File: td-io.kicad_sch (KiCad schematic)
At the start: 156 parts, among them J1 USB_A, J2 USB_B, J3 JAMMA_Edge, J4 Conn_Coaxial_x2, J5 DB15_Female_HighDensity_Mount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, J6 Conn_02x04_Top_Bottom, J7 Conn_02x17_Odd_Even, J8 Conn_01x05_Male, J9 Conn_01x04_Male, Q1 AO4818B, Q2 AO4818B, Q3 AO4818B, Q4 2N7002NXBKR, Q5 2N7002NXBKR, Q6 2N7002NXBKR, SW1 SW_DPDT_x2, SW2 SW_DPDT_x2, SW3 SW_DPDT_x2, U1 TPA3138D2, U10 Pico, U11 MAX860, U12 CPC1017N, U13 74LS165, U14 TPS259620, U15 LM2903, U16 PCA9306D, U2 ISL3175EIBZ-T, U3 ADA4861-3, U4 74LS86, U5 AT24CS01-SSHM, U6 74LS165, U7 TPS568230, U8 74LS165, U9 74LS165

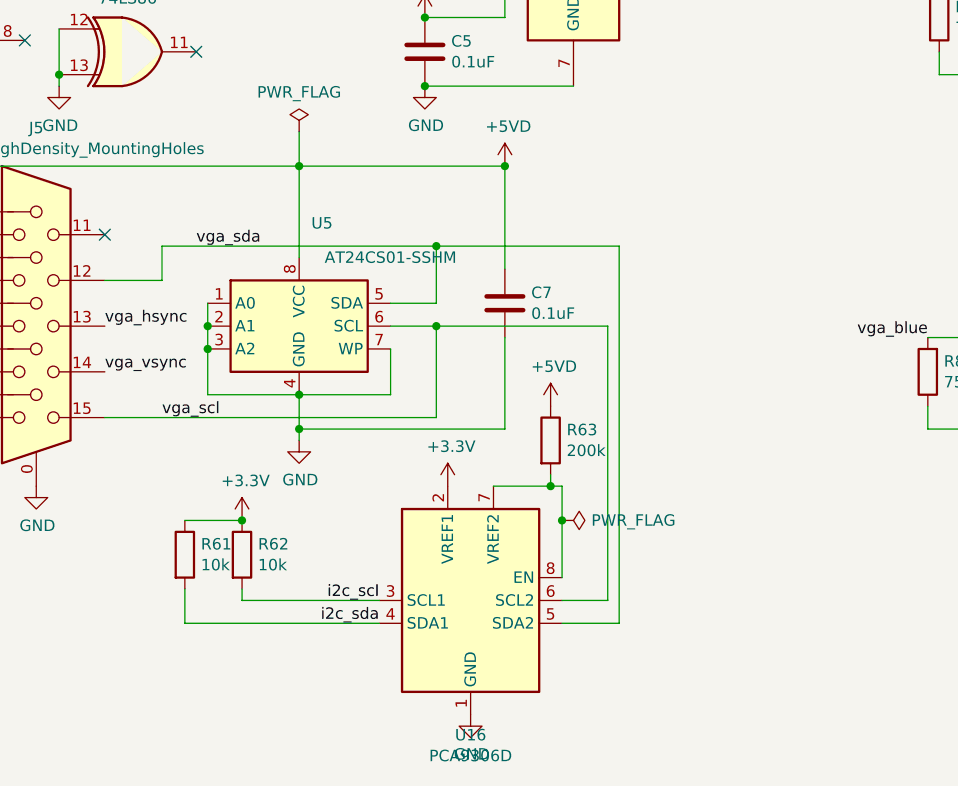
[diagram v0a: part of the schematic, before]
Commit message: drop i2c rom
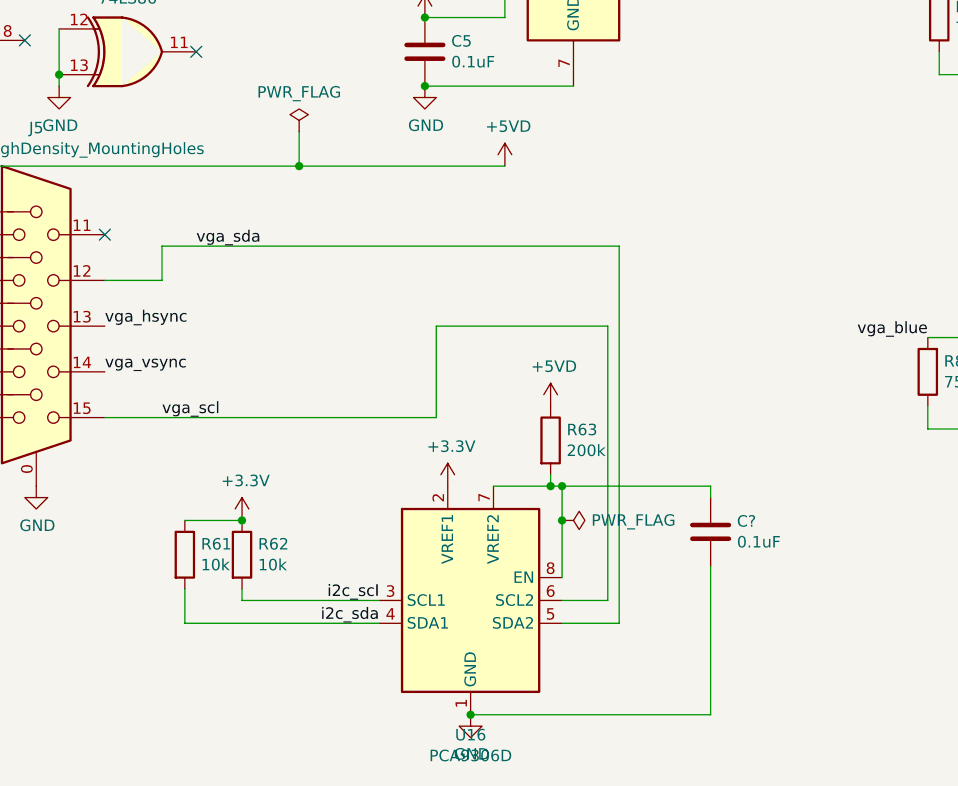
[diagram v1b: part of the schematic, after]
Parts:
- removed C7: 0.1uF, Capacitor_SMD:C_0805_2012Metric, symbol Device:C
- removed U5: AT24CS01-SSHM, Package_SO:SOIC-8_3.9x4.9mm_P1.27mm, symbol Memory_EEPROM:AT24CS01-SSHM
- added C?: 0.1uF, Capacitor_SMD:C_0805_2012Metric, symbol Device:C
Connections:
- net GND: now also C?.2
- net at R63.2, U16.7 (VREF2), U16.8 (EN): now also C?.1

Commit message: some pcb layout action
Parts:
- gave numbers to parts that had none: 1
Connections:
- net at F5.2, Q2.7 (D1), Q2.8 (D1): now also D4.2 (K); no longer D3.1 (K)
- net at F3.2, Q3.5 (D2), Q3.6 (D2): now also D3.1 (K); no longer D4.2 (K)
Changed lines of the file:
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@@
   (junction (at 524.51 62.23) (diameter 0) (color 0 0 0 0)
   )
-  (junction (at 481.33 143.51) (diameter 0) (color 0 0 0 0)
-  )
   (junction (at 506.73 58.42) (diameter 0) (color 0 0 0 0)
   )
@@
   (junction (at 419.1 45.72) (diameter 0) (color 0 0 0 0)
   )
+  (junction (at 481.33 143.51) (diameter 0) (color 0 0 0 0)
+  )
   (junction (at 41.91 367.03) (diameter 0) (color 0 0 0 0)
   )
@@
   (junction (at 405.13 210.82) (diameter 0) (color 0 0 0 0)
   )
-  (junction (at 452.755 182.88) (diameter 0) (color 0 0 0 0)
-  )
   (junction (at 207.01 378.46) (diameter 0) (color 0 0 0 0)
   )
@@
   (junction (at 87.63 95.25) (diameter 0) (color 0 0 0 0)
   )
+  (junction (at 452.755 182.88) (diameter 0) (color 0 0 0 0)
+  )
   (junction (at 222.25 363.22) (diameter 0) (color 0 0 0 0)
   )
@@
     (stroke (width 0) (type default) (color 0 0 0 0))
   )
+  (wire (pts (xy 452.755 182.88) (xy 465.455 182.88))
+    (stroke (width 0) (type default) (color 0 0 0 0))
+  )
   (wire (pts (xy 472.44 143.51) (xy 472.44 127))
     (stroke (width 0) (type default) (color 0 0 0 0))
@@
     (stroke (width 0) (type default) (color 0 0 0 0))
   )
+  (wire (pts (xy 495.935 166.37) (xy 495.935 143.51))
+    (stroke (width 0) (type default) (color 0 0 0 0))
+  )
   (wire (pts (xy 38.1 21.59) (xy 38.1 46.99))
     (stroke (width 0) (type default) (color 0 0 0 0))
@@
     (stroke (width 0) (type default) (color 0 0 0 0))
   )
+  (wire (pts (xy 495.935 166.37) (xy 511.175 166.37))
+    (stroke (width 0) (type default) (color 0 0 0 0))
+  )
   (wire (pts (xy 510.54 127) (xy 510.54 142.875))
     (stroke (width 0) (type default) (color 0 0 0 0))
@@
     (stroke (width 0) (type default) (color 0 0 0 0))
   )
+  (wire (pts (xy 505.46 142.875) (xy 499.745 142.875))
+    (stroke (width 0) (type default) (color 0 0 0 0))
+  )
   (wire (pts (xy 560.07 44.45) (xy 560.07 48.26))
     (stroke (width 0) (type default) (color 0 0 0 0))
@@
     (stroke (width 0) (type default) (color 0 0 0 0))
   )
-  (wire (pts (xy 452.755 182.88) (xy 470.535 182.88))
-    (stroke (width 0) (type default) (color 0 0 0 0))
-  )
   (wire (pts (xy 388.62 182.88) (xy 388.62 173.99))
     (stroke (width 0) (type default) (color 0 0 0 0))
@@
     (stroke (width 0) (type default) (color 0 0 0 0))
   )
-  (wire (pts (xy 501.65 143.51) (xy 501.65 142.875))
-    (stroke (width 0) (type default) (color 0 0 0 0))
-  )
   (wire (pts (xy 444.5 50.8) (xy 444.5 45.72))
     (stroke (width 0) (type default) (color 0 0 0 0))
@@
     (stroke (width 0) (type default) (color 0 0 0 0))
   )
-  (wire (pts (xy 470.535 166.37) (xy 470.535 182.88))
+  (wire (pts (xy 465.455 165.1) (xy 465.455 182.88))
     (stroke (width 0) (type default) (color 0 0 0 0))
   )
@@
     (stroke (width 0) (type default) (color 0 0 0 0))
   )
+  (wire (pts (xy 495.935 143.51) (xy 481.33 143.51))
+    (stroke (width 0) (type default) (color 0 0 0 0))
+  )
   (wire (pts (xy 161.29 368.3) (xy 161.29 370.84))
     (stroke (width 0) (type default) (color 0 0 0 0))
@@
     (stroke (width 0) (type default) (color 0 0 0 0))
   )
-  (wire (pts (xy 481.33 143.51) (xy 501.65 143.51))
-    (stroke (width 0) (type default) (color 0 0 0 0))
-  )
   (wire (pts (xy 208.28 326.39) (xy 208.28 339.09))
     (stroke (width 0) (type default) (color 0 0 0 0))
@@
     (stroke (width 0) (type default) (color 0 0 0 0))
   )
+  (wire (pts (xy 499.745 165.1) (xy 465.455 165.1))
+    (stroke (width 0) (type default) (color 0 0 0 0))
+  )
   (wire (pts (xy 60.96 97.79) (xy 60.96 86.36))
     (stroke (width 0) (type default) (color 0 0 0 0))
@@
     (stroke (width 0) (type default) (color 0 0 0 0))
   )
-  (wire (pts (xy 470.535 166.37) (xy 511.175 166.37))
-    (stroke (width 0) (type default) (color 0 0 0 0))
-  )
   (wire (pts (xy 276.86 90.17) (xy 280.67 90.17))
     (stroke (width 0) (type default) (color 0 0 0 0))
@@
     (stroke (width 0) (type default) (color 0 0 0 0))
   )
-  (wire (pts (xy 501.65 142.875) (xy 505.46 142.875))
-    (stroke (width 0) (type default) (color 0 0 0 0))
-  )
   (wire (pts (xy 110.49 402.59) (xy 137.16 402.59))
     (stroke (width 0) (type default) (color 0 0 0 0))
@@
     (stroke (width 0) (type default) (color 0 0 0 0))
   )
+  (wire (pts (xy 499.745 142.875) (xy 499.745 165.1))
+    (stroke (width 0) (type default) (color 0 0 0 0))
+  )
   (wire (pts (xy 50.8 21.59) (xy 57.15 21.59))
     (stroke (width 0) (type default) (color 0 0 0 0))
@@
   (symbol (lib_id "Device:C") (at 137.16 382.27 0) (unit 1)
     (in_bom yes) (on_board yes)
-    (property "Reference" "C?" (id 0) (at 140.081 381.1016 0)
+    (property "Reference" "C7" (id 0) (at 140.081 381.1016 0)
       (effects (font (size 1.27 1.27)) (justify left))
     )
@@
   (symbol (lib_id "power:GND") (at 100.33 285.75 0) (unit 1)
     (in_bom yes) (on_board yes)
-    (property "Reference" "#PWR?" (id 0) (at 100.33 292.1 0)
+    (property "Reference" "#PWR0127" (id 0) (at 100.33 292.1 0)
       (effects (font (size 1.27 1.27)) hide)
     )
@@
       (reference "#PWR0126") (unit 1) (value "+5V") (footprint "")
     )
+    (path "/ea8e2432-37dd-41a8-b7a1-d69d5340706c"
+      (reference "#PWR0127") (unit 1) (value "GND") (footprint "")
+    )
     (path "/00000000-0000-0000-0000-000060061134"
       (reference "#PWR0128") (unit 1) (value "GND") (footprint "")
@@
       (reference "#PWR0179") (unit 1) (value "+3.3V") (footprint "")
     )
-    (path "/ea8e2432-37dd-41a8-b7a1-d69d5340706c"
-      (reference "#PWR?") (unit 1) (value "GND") (footprint "")
-    )
     (path "/00000000-0000-0000-0000-000060392eef"
       (reference "C1") (unit 1) (value "1uF") (footprint "Capacitor_SMD:C_0805_2012Metric")
@@
       (reference "C6") (unit 1) (value "0.1uF") (footprint "Capacitor_SMD:C_0805_2012Metric")
     )
+    (path "/6fed136c-eb32-480f-be11-cce40318add5"
+      (reference "C7") (unit 1) (value "0.1uF") (footprint "Capacitor_SMD:C_0805_2012Metric")
+    )
     (path "/00000000-0000-0000-0000-000060403e55"
       (reference "C8") (unit 1) (value "1uF") (footprint "Capacitor_SMD:C_0805_2012Metric")
@@
       (reference "C40") (unit 1) (value "1uF") (footprint "Capacitor_SMD:C_0805_2012Metric")
     )
-    (path "/6fed136c-eb32-480f-be11-cce40318add5"
-      (reference "C?") (unit 1) (value "0.1uF") (footprint "Capacitor_SMD:C_0805_2012Metric")
-    )
     (path "/00000000-0000-0000-0000-000061046d38"

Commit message: finish layout
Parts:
- removed JP1: Jumper_NC_Small, Jumper:SolderJumper-2_P1.3mm_Bridged_RoundedPad1.0x1.5mm, symbol Device:Jumper_NC_Small
- removed R2: 400k, Resistor_SMD:R_0805_2012Metric, symbol Device:R
- removed R3: 1k, Resistor_SMD:R_0805_2012Metric, symbol Device:R
- removed U14: TPS259620, Package_SO:SOIC-8-1EP_3.9x4.9mm_P1.27mm_EP2.41x3.3mm_ThermalVias, symbol td-io:TPS259631
- added F6: Polyfuse, Resistor_SMD:R_1812_4532Metric, symbol Device:Polyfuse
- RV1: symbol Device:R_POT_Dual -> Device:R_Potentiometer_Dual
- U10: footprint td-io:RPi_Pico_SMD -> RPi_Pico:RPi_Pico_SMD_TH
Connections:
- net +5V: now also F6.2
- net +5VD: now also D2.1
- net +5VL: now also F6.1
- no-connect marks 64 -> 63

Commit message: update to new psu
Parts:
- removed C10: 1uF, Capacitor_SMD:C_0805_2012Metric, symbol Device:C
- removed C11, C29: 0.1uF, Capacitor_SMD:C_0805_2012Metric, symbol Device:C
- removed C12, C9: 100uF, Capacitor_SMD:C_1210_3225Metric, symbol Device:C
- removed L1: 1.5uH, Inductor_SMD:L_Bourns_SRP7028A_7.3x6.6mm, symbol Device:L
- removed R20: 300k, Resistor_SMD:R_0805_2012Metric, symbol Device:R
- removed R21: 43k, Resistor_SMD:R_0805_2012Metric, symbol Device:R
- removed R32: 1k, Resistor_SMD:R_0805_2012Metric, symbol Device:R
- removed R33: 220, Resistor_SMD:R_0805_2012Metric, symbol Device:R
- removed U7: TPS568230, td-io:RJE-20, symbol td-io:TPS568230
- D2: Digikey (none) -> BAT54CFSCT-ND
- J8: value Conn_01x05_Male -> DNP
- R11, R12, R13: JLCPCB (none) -> C17630; LCSC (none) -> C17630
- R61, R62: Digikey (none) -> 311-10.0KCRCT-ND
- R63: Digikey (none) -> 311-200KCRCT-ND; JLCPCB (none) -> C17539; LCSC (none) -> C17539
- U13, U6, U8, U9: value 74LS165 -> 74LV165
- U16: Digikey (none) -> 568-4215-1-ND
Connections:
- no-connect marks 63 -> 61
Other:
- added sheet JVS Power (jvs-power.kicad_sch)

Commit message: small fixes
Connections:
- net +3V3: no longer R22.1, R23.1, R24.1, R27.1, R28.1, R29.1, R30.1, R31.1, R34.1, R35.1, R36.1, R37.1, R38.1, R39.1, R40.1, R41.1, R42.1, R43.1, R44.1, R45.1, R46.1, R47.1, R48.1, R49.1, R56.1, R57.1, R58.1, U13.14 (D3), U13.3 (D4), U13.4 (D5), U13.5 (D6), U13.6 (D7)
- net +5V: now also R22.1, R23.1, R24.1, R27.1, R28.1, R29.1, R30.1, R31.1, R34.1, R35.1, R36.1, R37.1, R38.1, R39.1, R40.1, R41.1, R42.1, R43.1, R44.1, R45.1, R46.1, R47.1, R48.1, R49.1, R56.1, R57.1, R58.1, U13.14 (D3), U13.3 (D4), U13.4 (D5), U13.5 (D6), U13.6 (D7)

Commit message: re test zones
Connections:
- net +3V3: now also U13.14 (D3), U13.3 (D4), U13.4 (D5), U13.5 (D6), U13.6 (D7)
- net +5V: no longer U13.14 (D3), U13.3 (D4), U13.4 (D5), U13.5 (D6), U13.6 (D7)
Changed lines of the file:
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@@
   (junction (at 41.91 369.57) (diameter 0) (color 0 0 0 0)
   )
+  (junction (at 40.64 21.59) (diameter 0) (color 0 0 0 0)
+  )
   (junction (at 175.26 360.68) (diameter 0) (color 0 0 0 0)
   )
@@
   (junction (at 102.87 172.72) (diameter 0) (color 0 0 0 0)
   )
-  (junction (at 46.6093 21.59) (diameter 0) (color 0 0 0 0)
-  )
   (junction (at 138.43 105.41) (diameter 0) (color 0 0 0 0)
   )
@@
   (junction (at 105.41 325.12) (diameter 0) (color 0 0 0 0)
   )
-  (junction (at 50.8 21.59) (diameter 0) (color 0 0 0 0)
-  )
   (junction (at 513.08 102.87) (diameter 0) (color 0 0 0 0)
   )
@@
   (junction (at 388.62 173.99) (diameter 0) (color 0 0 0 0)
   )
-  (junction (at 57.15 21.59) (diameter 0) (color 0 0 0 0)
-  )
   (junction (at 134.62 97.79) (diameter 0) (color 0 0 0 0)
   )
+  (junction (at 58.42 21.59) (diameter 0) (color 0 0 0 0)
+  )
   (junction (at 344.17 95.25) (diameter 0) (color 0 0 0 0)
   )
@@
     (stroke (width 0) (type default) (color 0 0 0 0))
   )
+  (wire (pts (xy 40.64 21.59) (xy 44.45 21.59))
+    (stroke (width 0) (type default) (color 0 0 0 0))
+  )
   (wire (pts (xy 269.24 64.77) (xy 269.24 74.93))
     (stroke (width 0) (type default) (color 0 0 0 0))
@@
     (stroke (width 0) (type default) (color 0 0 0 0))
   )
-  (wire (pts (xy 46.6093 21.59) (xy 50.8 21.59))
+  (wire (pts (xy 44.45 21.59) (xy 50.8 21.59))
     (stroke (width 0) (type default) (color 0 0 0 0))
   )
@@
     (stroke (width 0) (type default) (color 0 0 0 0))
   )
-  (wire (pts (xy 38.1 21.59) (xy 44.45 21.59))
+  (wire (pts (xy 38.1 21.59) (xy 40.64 21.59))
     (stroke (width 0) (type default) (color 0 0 0 0))
   )
@@
     (stroke (width 0) (type default) (color 0 0 0 0))
   )
-  (wire (pts (xy 57.15 21.59) (xy 63.5 21.59))
+  (wire (pts (xy 57.15 21.59) (xy 58.42 21.59))
     (stroke (width 0) (type default) (color 0 0 0 0))
   )
@@
     (stroke (width 0) (type default) (color 0 0 0 0))
   )
-  (wire (pts (xy 44.45 21.59) (xy 46.6093 21.59))
-    (stroke (width 0) (type default) (color 0 0 0 0))
-  )
   (wire (pts (xy 273.05 125.73) (xy 260.35 125.73))
     (stroke (width 0) (type default) (color 0 0 0 0))
@@
     (stroke (width 0) (type default) (color 0 0 0 0))
   )
+  (wire (pts (xy 58.42 21.59) (xy 63.5 21.59))
+    (stroke (width 0) (type default) (color 0 0 0 0))
+  )
   (wire (pts (xy 176.53 292.1) (xy 168.91 292.1))
     (stroke (width 0) (type default) (color 0 0 0 0))
@@
     (stroke (width 0) (type default) (color 0 0 0 0))
   )
-  (wire (pts (xy 50.8 21.59) (xy 57.15 21.59))
-    (stroke (width 0) (type default) (color 0 0 0 0))
-  )
   (wire (pts (xy 345.44 156.21) (xy 350.52 156.21))
     (stroke (width 0) (type default) (color 0 0 0 0))
@@
   (symbol (lib_id "power:+5V") (at 142.24 21.59 0) (unit 1)
     (in_bom yes) (on_board yes)
-    (property "Reference" "#PWR?" (id 0) (at 142.24 25.4 0)
+    (property "Reference" "#PWR0174" (id 0) (at 142.24 25.4 0)
       (effects (font (size 1.27 1.27)) hide)
     )
@@
   (symbol (lib_id "power:+5V") (at 234.95 21.59 0) (unit 1)
     (in_bom yes) (on_board yes)
-    (property "Reference" "#PWR?" (id 0) (at 234.95 25.4 0)
+    (property "Reference" "#PWR0180" (id 0) (at 234.95 25.4 0)
       (effects (font (size 1.27 1.27)) hide)
     )
@@
   (symbol (lib_id "power:+5V") (at 326.39 21.59 0) (unit 1)
     (in_bom yes) (on_board yes)
-    (property "Reference" "#PWR?" (id 0) (at 326.39 25.4 0)
+    (property "Reference" "#PWR0181" (id 0) (at 326.39 25.4 0)
       (effects (font (size 1.27 1.27)) hide)
     )
@@
     (pin "1")
   )
-  (symbol (lib_id "power:+5V") (at 46.6093 21.59 0) (unit 1)
+  (symbol (lib_id "power:+3.3V") (at 40.64 21.59 0) (unit 1)
     (in_bom yes) (on_board yes)
-    (property "Reference" "#PWR?" (id 0) (at 46.6093 25.4 0)
+    (property "Reference" "#PWR0182" (id 0) (at 40.64 25.4 0)
       (effects (font (size 1.27 1.27)) hide)
     )
-    (property "Value" "+5V" (id 1) (at 46.9903 17.1958 0))
-    (property "Footprint" "" (id 2) (at 46.6093 21.59 0)
+    (property "Value" "+3.3V" (id 1) (at 41.021 17.1958 0))
+    (property "Footprint" "" (id 2) (at 40.64 21.59 0)
       (effects (font (size 1.27 1.27)) hide)
     )
-    (property "Datasheet" "" (id 3) (at 46.6093 21.59 0)
+    (property "Datasheet" "" (id 3) (at 40.64 21.59 0)
+      (effects (font (size 1.27 1.27)) hide)
+    )
+    (pin "1")
+  )
+  (symbol (lib_id "power:+5V") (at 58.42 21.59 0) (unit 1)
+    (in_bom yes) (on_board yes)
+    (property "Reference" "#PWR0170" (id 0) (at 58.42 25.4 0)
+      (effects (font (size 1.27 1.27)) hide)
+    )
+    (property "Value" "+5V" (id 1) (at 58.801 17.1958 0))
+    (property "Footprint" "" (id 2) (at 58.42 21.59 0)
+      (effects (font (size 1.27 1.27)) hide)
+    )
+    (property "Datasheet" "" (id 3) (at 58.42 21.59 0)
       (effects (font (size 1.27 1.27)) hide)
     )
@@
       (reference "#PWR0169") (unit 1) (value "+5VL") (footprint "")
     )
+    (path "/ffe22384-e883-4e1b-8ea5-8cd9920b7e29"
+      (reference "#PWR0170") (unit 1) (value "+5V") (footprint "")
+    )
     (path "/00000000-0000-0000-0000-0000618aaa02"
       (reference "#PWR0171") (unit 1) (value "+5VL") (footprint "")
@@
       (reference "#PWR0173") (unit 1) (value "+5V") (footprint "")
     )
+    (path "/0fbe2b74-1168-4ba2-a970-ad39200fbfe3"
+      (reference "#PWR0174") (unit 1) (value "+5V") (footprint "")
+    )
     (path "/00000000-0000-0000-0000-0000623f55c5"
       (reference "#PWR0175") (unit 1) (value "+12V") (footprint "")
@@
       (reference "#PWR0179") (unit 1) (value "+3.3V") (footprint "")
     )
-    (path "/0fbe2b74-1168-4ba2-a970-ad39200fbfe3"
-      (reference "#PWR?") (unit 1) (value "+5V") (footprint "")
-    )
     (path "/428f80bb-e0ea-4a27-ad95-4a82535e78f0"
-      (reference "#PWR?") (unit 1) (value "+5V") (footprint "")
+      (reference "#PWR0180") (unit 1) (value "+5V") (footprint "")
     )
     (path "/d1c39b30-5daa-46af-a8a1-9843ba656069"
-      (reference "#PWR?") (unit 1) (value "+5V") (footprint "")
+      (reference "#PWR0181") (unit 1) (value "+5V") (footprint "")
     )
-    (path "/ffe22384-e883-4e1b-8ea5-8cd9920b7e29"
-      (reference "#PWR?") (unit 1) (value "+5V") (footprint "")
+    (path "/f720d303-6cc4-484c-8533-ce7385e4e7a8"
+      (reference "#PWR0182") (unit 1) (value "+3.3V") (footprint "")
     )
     (path "/00000000-0000-0000-0000-000060392eef"
